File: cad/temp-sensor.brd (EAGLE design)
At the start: 100 x 80 mm, 64 parts, among them Q1 300S14-U, Q2 320S14-U, Q3 320S14-U, U1 SE555D, U2 SE555D, U4 MCP6001UT-I/OT, U5 MCP6001UT-I/OT, U6 MCP6001UT-I/OT, U7 MCP6001UT-I/OT, U8 NCV4264-2CST50T3G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

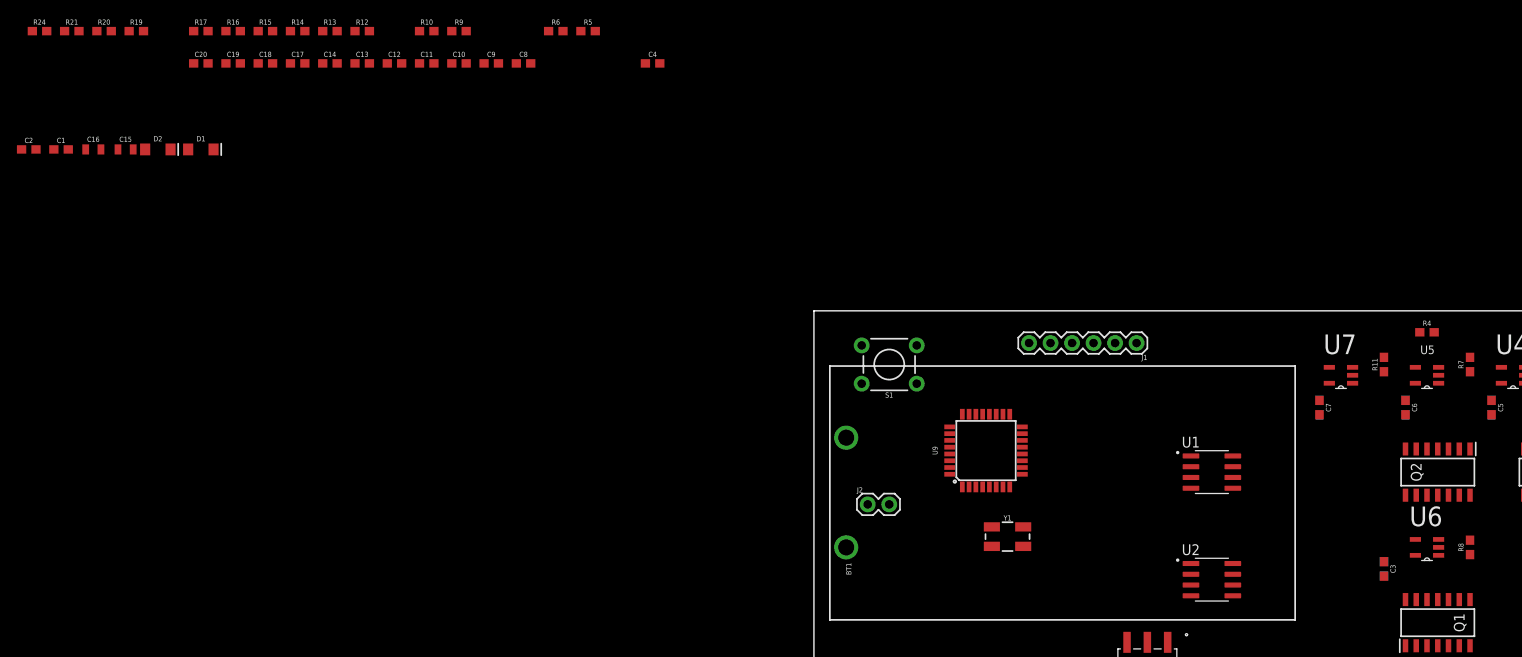
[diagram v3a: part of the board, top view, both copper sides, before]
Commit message: Finalized Schematic and Layout
Got rid of C11 and C13 since they were causing oscillations
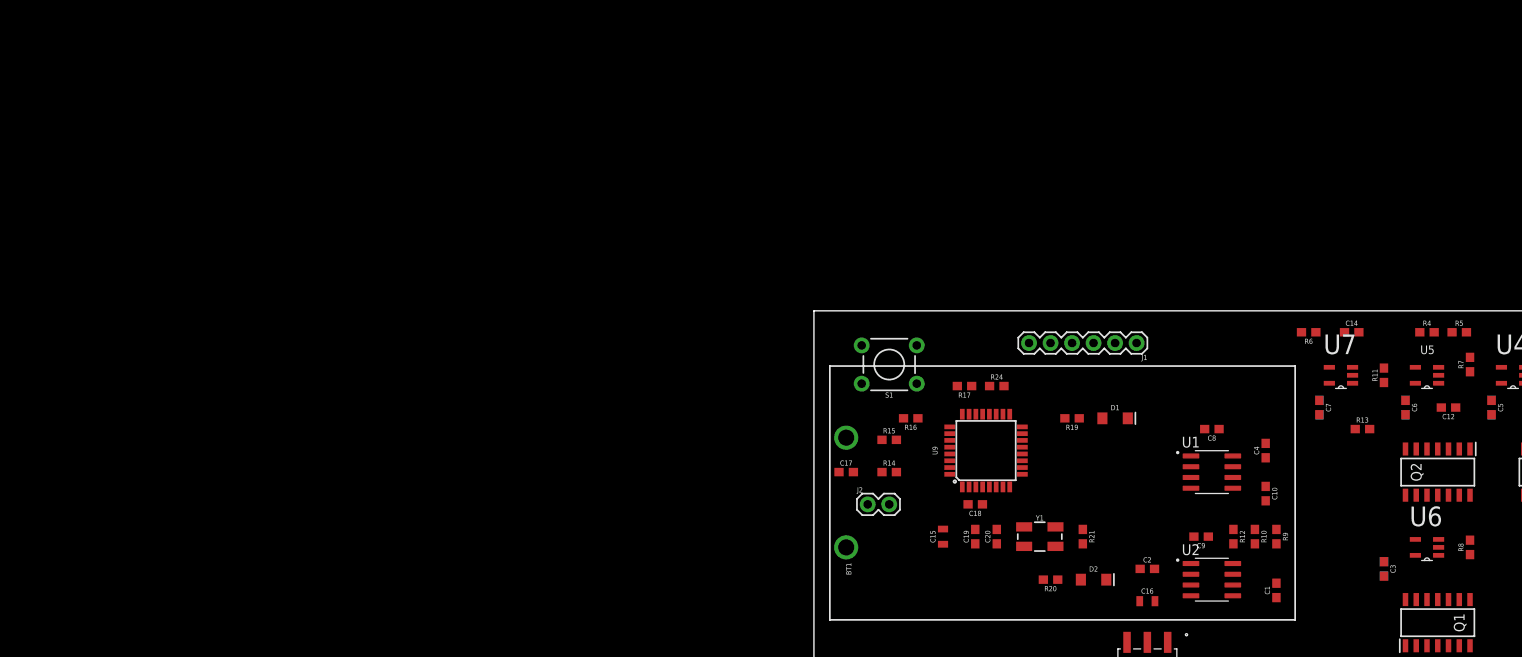
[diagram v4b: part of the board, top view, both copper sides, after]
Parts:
- removed C11, C13: 10nF, SparkFun-Capacitors:0603
- moved C1 152.7 mm to (54.6, 47.0), turned to 90 degrees
- moved C2 141.1 mm to (39.4, 49.5)
- moved C16 135.4 mm to (39.4, 45.7)
- moved R21 133.5 mm to (31.8, 53.3), turned to 270 degrees
- moved C12 130.9 mm to (74.9, 68.6), turned to 180 degrees
- moved R13 130.7 mm to (64.8, 66.0)
- moved R20 129.2 mm to (27.9, 48.3), turned to 180 degrees
- moved C14 124.8 mm to (63.5, 77.5)
- moved D2 121.6 mm to (33.0, 48.3)
- moved R24 120.5 mm to (21.6, 71.1)
- moved R19 119.6 mm to (30.5, 67.3), turned to 180 degrees
- moved R12 118.9 mm to (49.5, 53.3), turned to 270 degrees
- moved R10 114.6 mm to (52.1, 53.3), turned to 270 degrees
- moved R9 113.5 mm to (54.6, 53.3), turned to 270 degrees
- moved D1 112.5 mm to (35.6, 67.3)
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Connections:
- net BG_REF_FB: no longer C11.1
- net GND: no longer C11.2, C13.2
- net PTAT_REF_FB: no longer C13.1

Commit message: Finalized Layout
condensed board
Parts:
- moved R18 38.1 mm to (53.3, 50.8)
- moved U8 31.8 mm to (8.89, 47.0), turned to 90 degrees
- moved R2 30.5 mm to (63.5, 64.8), turned to 0 degrees
- moved Q3 29.3 mm to (58.4, 58.4)
- moved R4 29.2 mm to (43.2, 77.5)
- moved C24 28.0 mm to (39.4, 48.3)
- moved C3 28.0 mm to (39.4, 48.3)
- moved R8 28.0 mm to (49.5, 50.8)
- moved U6 28.0 mm to (44.5, 50.8)
- moved R5 27.9 mm to (48.3, 77.5)
- moved R1 27.4 mm to (63.5, 67.3), turned to 0 degrees
- moved Q2 26.8 mm to (47.0, 58.4)
- moved R13 25.9 mm to (39.4, 61.0)
- moved U4 25.0 mm to (58.4, 66.0)
- moved R3 24.4 mm to (63.5, 69.8), turned to 180 degrees
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
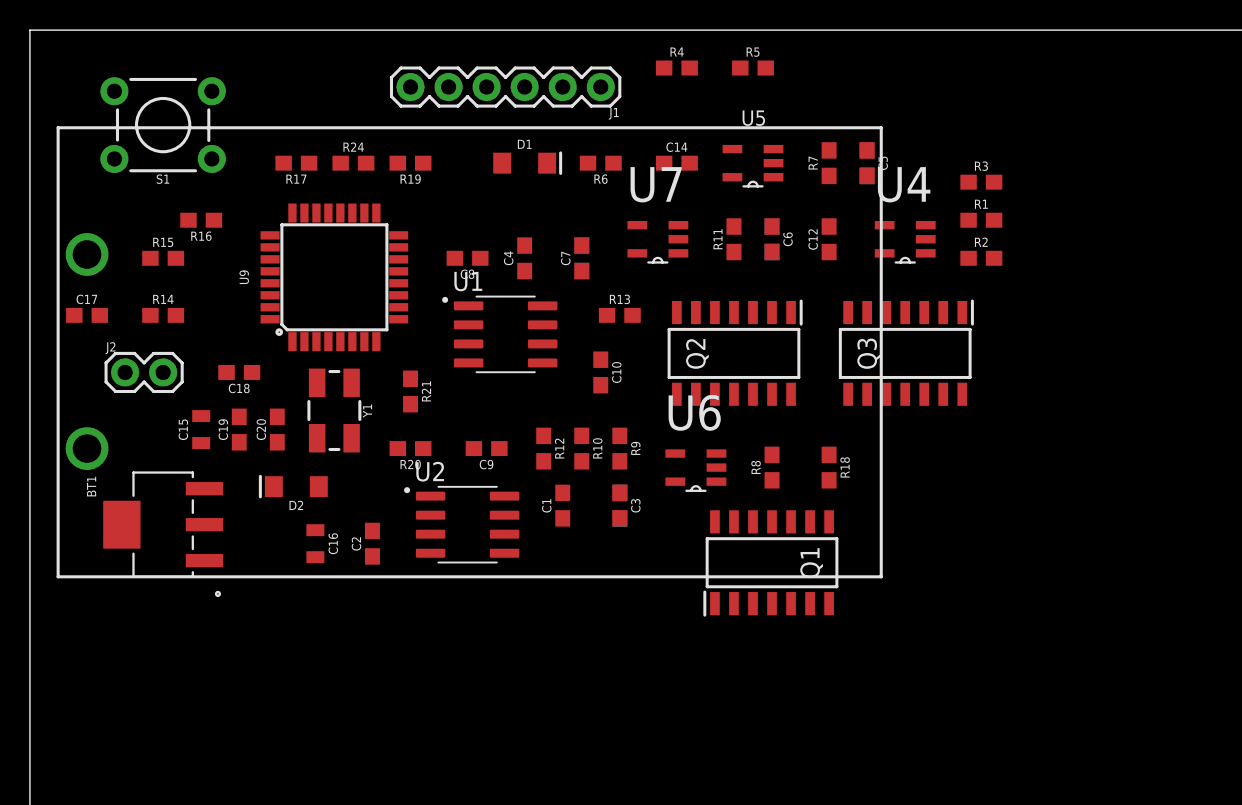
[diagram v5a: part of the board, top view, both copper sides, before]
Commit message: Edit placement
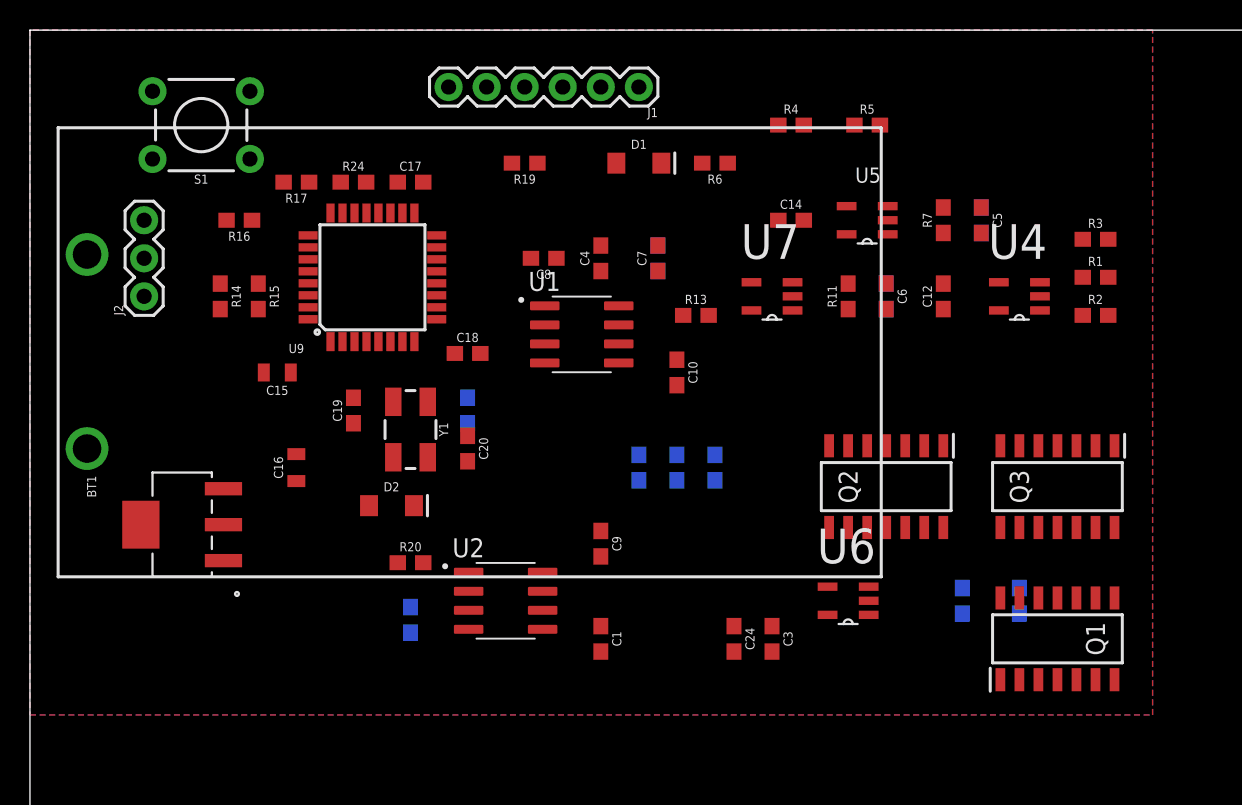
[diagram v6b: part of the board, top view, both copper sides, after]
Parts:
- J2: value (none) -> 455-1750-1-ND; device SparkFun-Connectors:1X02 -> SparkFun-Connectors:1X03
- moved C17 23.3 mm to (25.4, 69.8)
- moved Q1 19.7 mm to (68.6, 39.4)
- moved R18 15.5 mm to (66.0, 41.9), flipped to the bottom
- moved R8 15.5 mm to (62.2, 41.9), flipped to the bottom
- moved C18 15.3 mm to (29.2, 58.4), turned to 0 degrees
- moved C3 13.5 mm to (49.5, 39.4)
- moved Q2 13.5 mm to (57.1, 49.5)
- moved Q3 13.5 mm to (68.6, 49.5)
- moved U6 13.5 mm to (54.6, 41.9)
- moved C20 12.8 mm to (29.2, 52.1), turned to 270 degrees
- moved C24 11.7 mm to (47.0, 39.4), flipped to the top
- moved C9 9.92 mm to (38.1, 45.7), turned to 90 degrees
- moved C1 9.25 mm to (38.1, 39.4), turned to 270 degrees
- moved U4 8.52 mm to (66.0, 62.2)
- moved U7 8.52 mm to (49.5, 62.2)
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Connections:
- removed net N$1: C17.1
- net +5V: now also C17.1
- net GND: now also J2.3
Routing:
- added copper zone on layer 1, net +5V
- added copper zone on layer 16, net GND

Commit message: Edit placement again
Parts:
- moved Q1 33.0 mm to (68.6, 72.4), turned to 180 degrees
- moved U6 29.2 mm to (55.9, 71.1), turned to 0 degrees
- moved R8 29.2 mm to (62.2, 71.1), turned to 0 degrees
- moved R3 26.9 mm to (62.2, 40.6), turned to 0 degrees
- moved U8 26.7 mm to (10.2, 73.7), turned to 0 degrees
- moved C21 25.0 mm to (53.3, 44.5), turned to 90 degrees
- moved U4 23.9 mm to (55.9, 40.6), turned to 0 degrees
- moved C5 23.4 mm to (58.4, 44.5), turned to 90 degrees
- moved R1 22.2 mm to (62.2, 43.2), turned to 180 degrees
- moved R4 21.7 mm to (53.3, 52.1), flipped to the bottom, turned to 270 degrees
- moved R5 21.7 mm to (58.4, 52.1), flipped to the bottom, turned to 270 degrees
- moved C2 21.6 mm to (44.5, 50.8), flipped to the top, turned to 0 degrees
- moved R16 19.4 mm to (10.2, 48.3), flipped to the bottom, turned to 0 degrees
- moved R7 19.2 mm to (58.4, 48.3), flipped to the bottom, turned to 90 degrees
- moved C16 19.1 mm to (16.5, 69.8)
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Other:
- board text added: "GND"
- board text added: "SCL"
- board text added: "SDA"

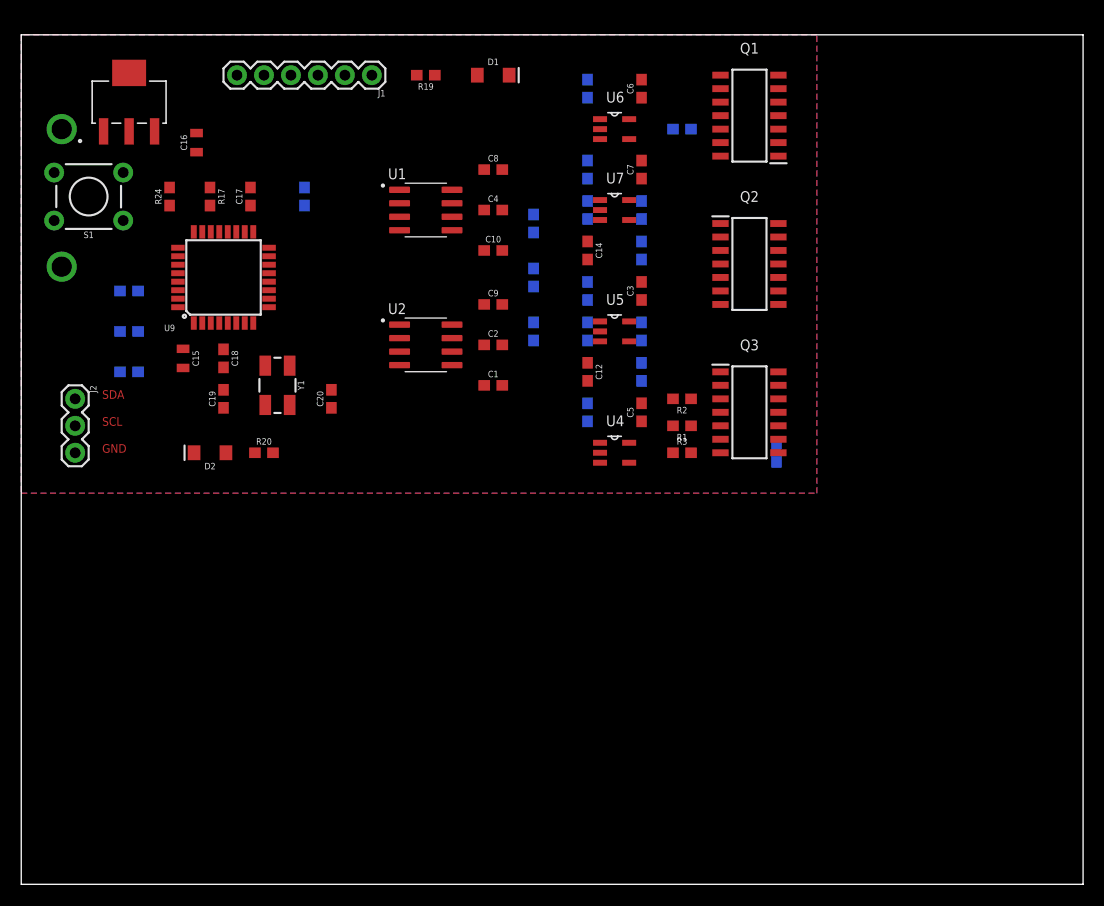
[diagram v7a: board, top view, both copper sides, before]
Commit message: Initial routing
Still need to add test points and clean up silk screen.
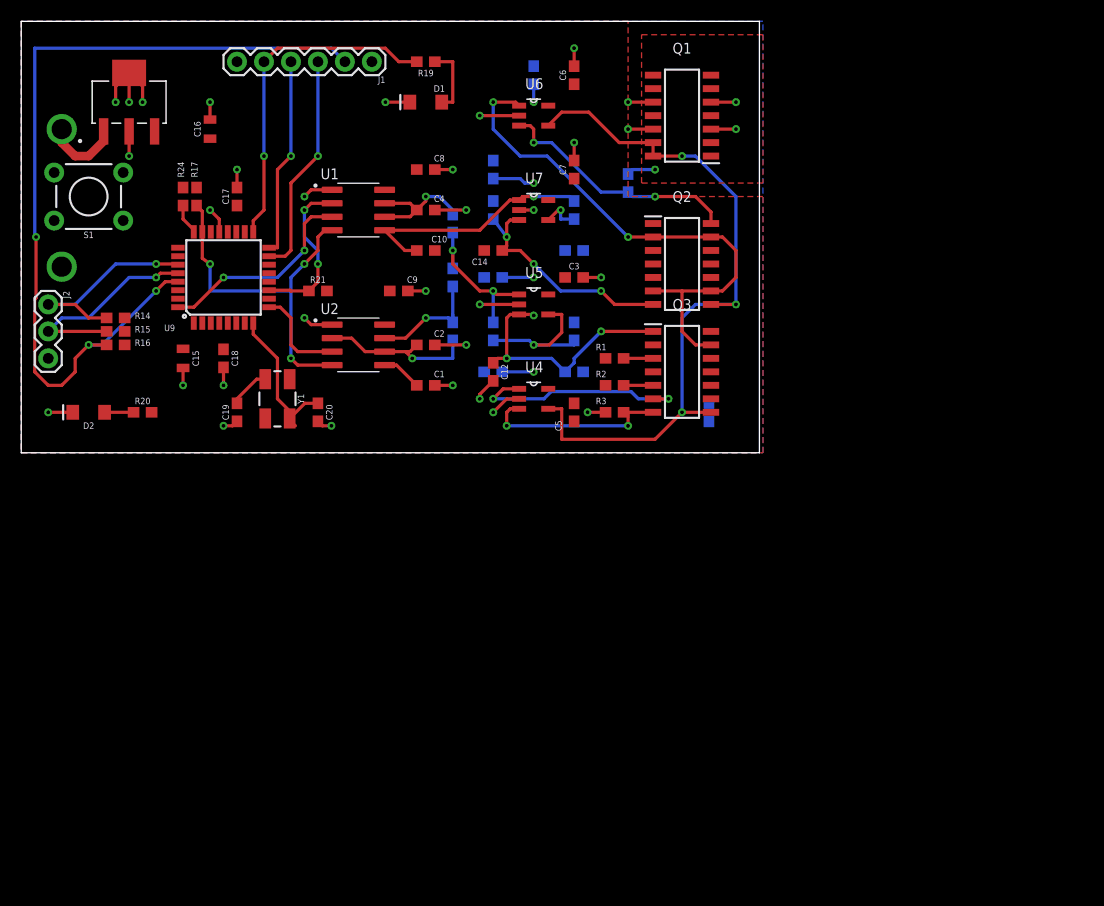
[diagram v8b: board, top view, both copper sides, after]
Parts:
- D1: value GREEN -> SCK
- D2: value GREEN -> POWER
- moved D2 12.0 mm to (6.35, 44.5)
- moved R20 12.0 mm to (11.4, 44.5)
- moved C21 9.67 mm to (44.5, 48.3), turned to 0 degrees
- moved J2 9.25 mm to (2.54, 54.6)
- moved U4 9.16 mm to (48.3, 45.7)
- moved C9 8.98 mm to (35.6, 55.9)
- moved C24 8.98 mm to (44.5, 57.1), turned to 0 degrees
- moved R1 8.98 mm to (55.9, 49.5)
- moved R21 8.98 mm to (27.9, 55.9), flipped to the top, turned to 0 degrees
- moved C12 8.89 mm to (44.5, 48.3)
- moved C14 8.89 mm to (44.5, 59.7), turned to 180 degrees
- moved C23 8.89 mm to (44.5, 67.3)
- moved R11 8.89 mm to (44.5, 63.5)
- moved R4 8.89 mm to (44.5, 52.1), turned to 90 degrees
- moved U5 8.03 mm to (48.3, 54.6)
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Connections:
- net CTAT_E1: now also R1.1; no longer R2.1
- net CTAT_E3: now also R2.1; no longer R1.1
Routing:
- net MCU_RST: track 0.00 -> 80.9 mm, vias 0 -> 3
- net GND: track 0.00 -> 75.1 mm, vias 0 -> 33
- net TEMP_VBE: track 0.00 -> 68.5 mm, vias 0 -> 3
- net PTAT_BASE: track 0.00 -> 50.6 mm, vias 0 -> 2
- net 555_RST_N: track 0.00 -> 34.5 mm, vias 0 -> 3
- net SCK: track 0.00 -> 31.9 mm, vias 0 -> 1
- net I_BG: track 0.00 -> 24.2 mm, vias 0 -> 3
- net VPTAT_REF: track 0.00 -> 23.6 mm, vias 0 -> 1
- net PTAT_IN+: track 0.00 -> 23.3 mm, vias 0 -> 2
- net I_PTAT: track 0.00 -> 22.4 mm, vias 0 -> 3
- net CTAT_BASE: track 0.00 -> 21.4 mm, vias 0 -> 2
- net COPI: track 0.00 -> 21.1 mm, vias 0 -> 1
- net SCL: track 0.00 -> 20.0 mm, vias 0 -> 1
- net SDA: track 0.00 -> 19.9 mm, vias 0 -> 1
- net PULSE_OUT: track 0.00 -> 19.5 mm, vias 0 -> 2
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- added copper zone on layer 1, net 3_NPN_DIODE
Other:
- board size 100 x 80 mm -> 69.5 x 40.6 mm
- board text removed: "GND"
- board text removed: "SCL"
- board text removed: "SDA"
